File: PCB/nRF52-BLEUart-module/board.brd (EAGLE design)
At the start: 39 x 18 mm, 44 parts, among them J1 USB-A_PTH_MALE, U1 CH340E, U2 NRF52832, Y1 32MHz_2016, Y2 32.768kHz

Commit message: fixed #4
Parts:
- moved C15 1.45 mm to (30.1, 8.64), turned to 315 degrees
- moved JP1 1.40 mm to (1.52, 9.00)
- moved C16 1.09 mm to (31.6, 11.7), turned to 135 degrees
- moved L1 0.40 mm to (30.9, 10.2), turned to 45 degrees
- moved C13 0.38 mm to (29.2, 10.8)
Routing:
- net VCCIO: track 23.1 -> 24.5 mm
- net UART_RX: track 29.8 -> 31.2 mm
- net RF-1: track 4.67 -> 3.52 mm
- net UART_TX: track 28.3 -> 28.9 mm

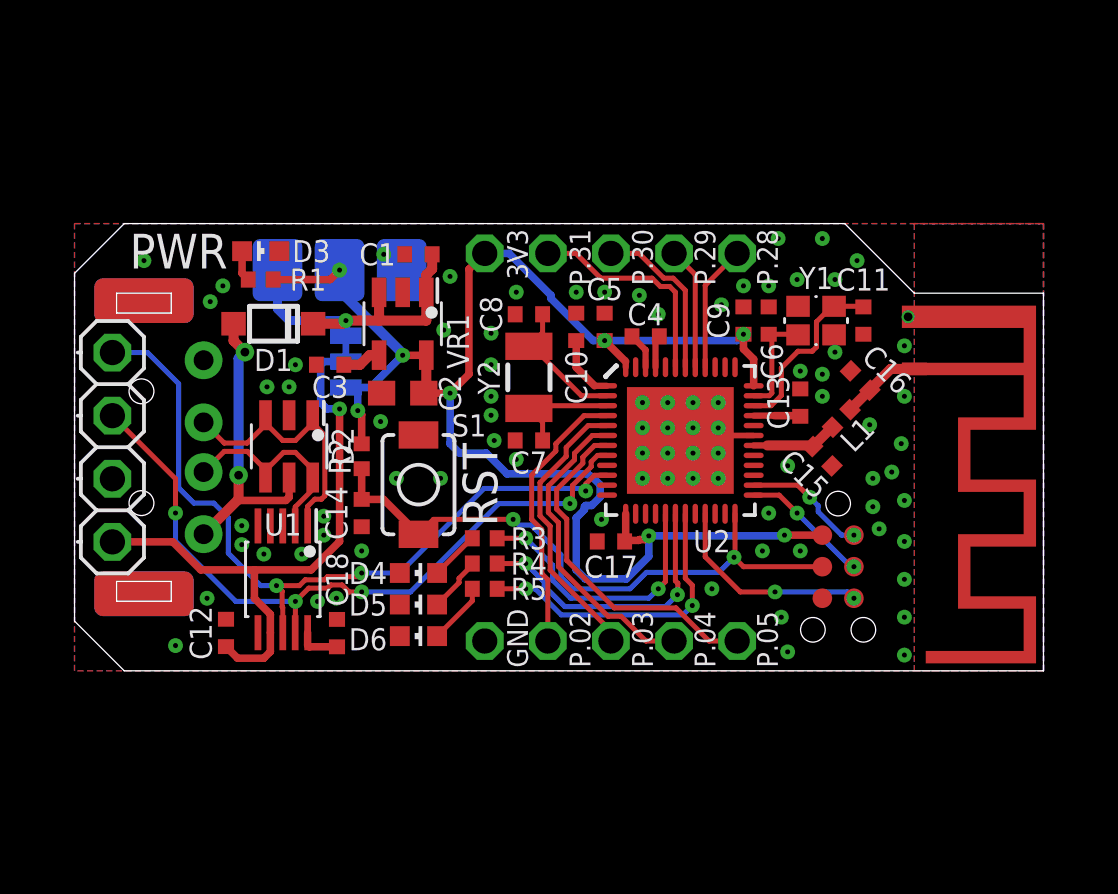
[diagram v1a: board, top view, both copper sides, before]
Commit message: fixed #2, removed unecessary power test pad
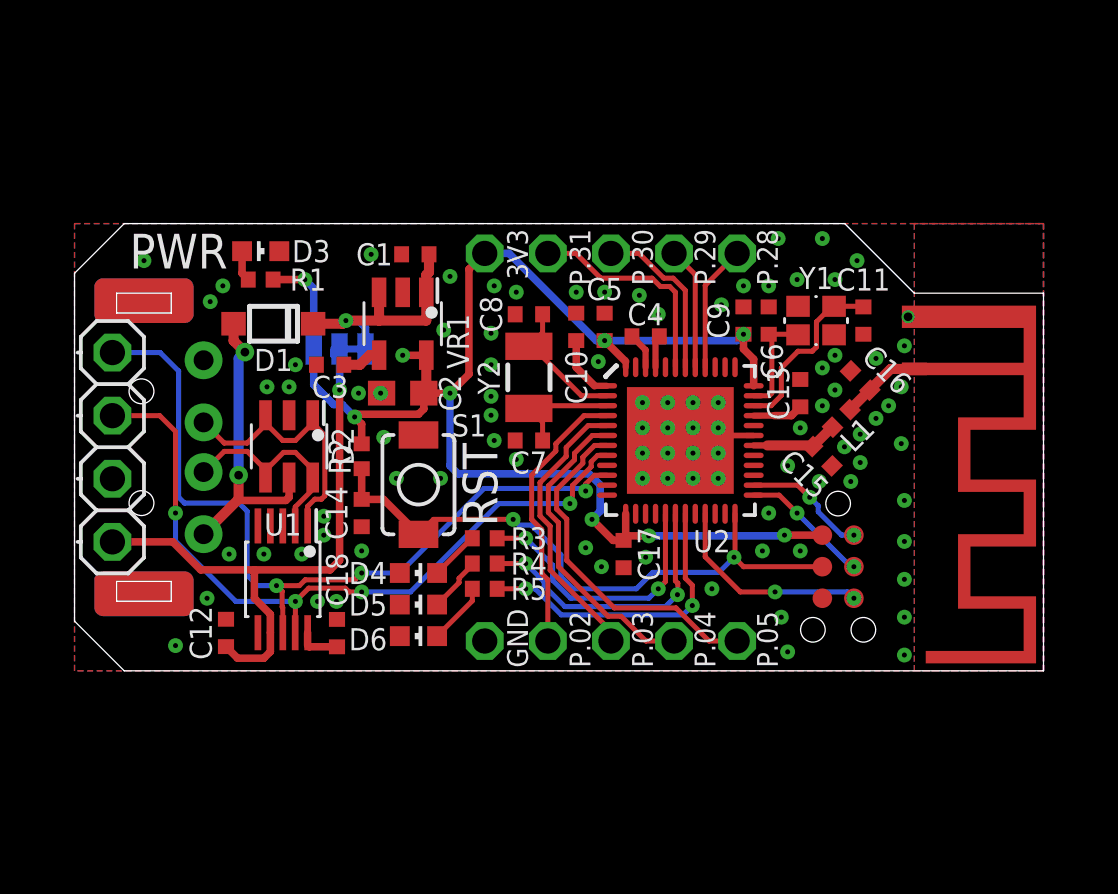
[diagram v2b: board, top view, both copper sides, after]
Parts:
- removed TP1: TEST-POINT-3, angrypig7-Tests:PAD-3X-RECT-SILK
- moved C17 0.72 mm to (22.1, 4.70), turned to 270 degrees
- moved JP2 0.57 mm to (10.7, 13.0), turned to 180 degrees
- moved C13 0.38 mm to (29.2, 11.2)
- moved C1 0.13 mm to (13.7, 16.8)
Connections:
- net 3V3: no longer TP1.P$2
- net 5V: no longer TP1.P$3
- net GND: no longer TP1.P$1
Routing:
- net 3V3: track 64.1 -> 59.6 mm, vias 8 -> 9
- net 5V: track 13.6 -> 10.2 mm
- net UART_RX: track 31.2 -> 32.4 mm
- net UART_TX: track 28.9 -> 29.9 mm
- net VCCIO: track 24.5 -> 24.0 mm
- net GND: vias 83 -> 92

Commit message: added edge rails, mousebites to the PCB. DRC error fixes needed
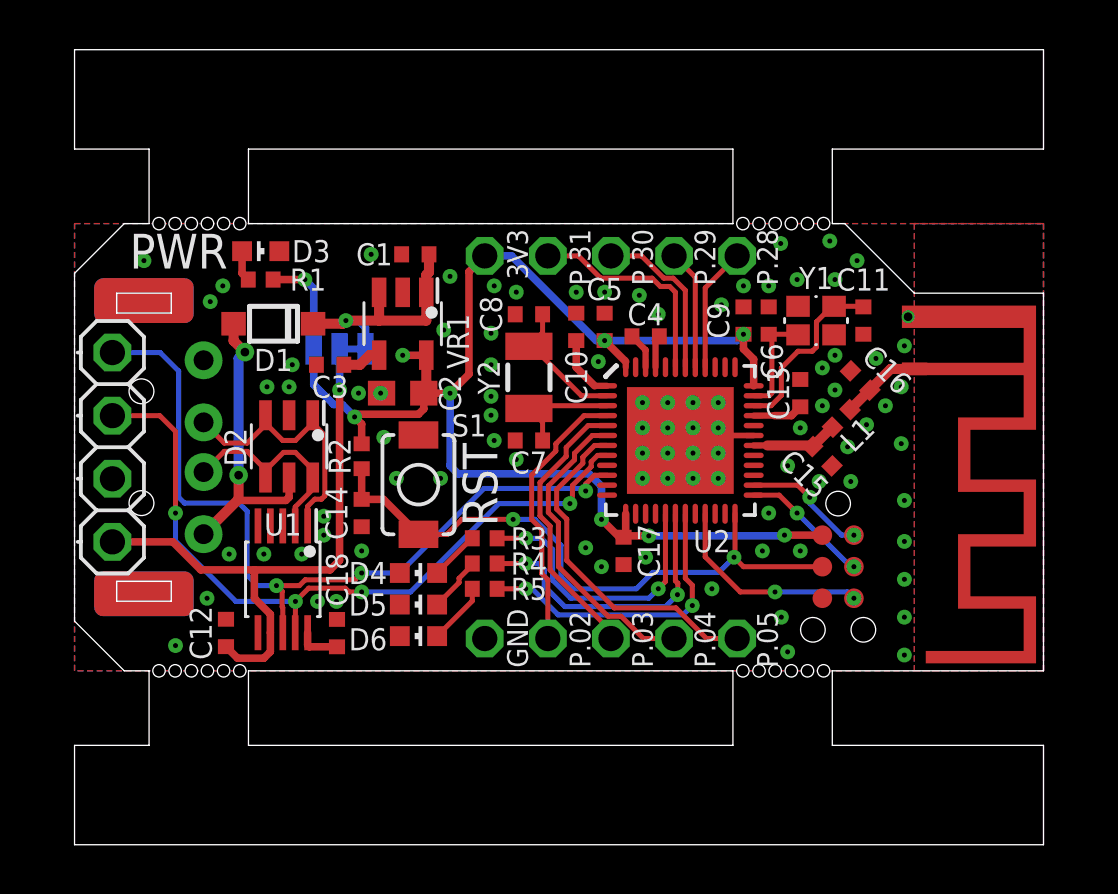
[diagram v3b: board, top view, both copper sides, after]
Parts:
- moved C17 0.13 mm to (22.1, 4.83)
- moved JP3 0.10 mm to (21.6, 16.7)
- moved JP4 0.10 mm to (21.6, 1.30)
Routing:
- net 3V3: track 59.6 -> 58.7 mm
- net GND: vias 92 -> 90
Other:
- board size 39 x 18 mm -> 39 x 32 mm

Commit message: PCB artwork, gerbers and production files - part rotation needs fixes
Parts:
- turned C12 to 270 degrees
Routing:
- net VCCIO: track 23.9 -> 23.1 mm
- net GND: vias 90 -> 88

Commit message: final PCB for V1.0
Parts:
- C15, C16: value (none) -> DNP
- JP1: device angrypig7-Connectors-PinHeads:1X04/90 -> angrypig7-Connectors-PinHeads:1X04-NOSILK
- JP2: value 3V3 5V -> 5V 3V3
- R1: value 10k -> 15k
- moved C12 1.05 mm to (6.35, 2.54)
- moved R1 0.68 mm to (8.13, 15.5)
- moved D3 0.68 mm to (8.13, 16.6)
- moved D1 0.54 mm to (8.38, 13.6)
- moved U1 0.13 mm to (8.51, 3.68)
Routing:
- net VCCIO: track 23.1 -> 22.1 mm
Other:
- board size 39 x 32 mm -> 41 x 32 mm
- board text added: ">CREVISION"

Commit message: V1.1.0 update
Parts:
- JP1: value V G Tx Rx -> Rx Tx G V
- R1: value 15k -> 7.5k
- U$1: device angrypig7-Antennas:TI-AN043_LEFT -> angrypig7-Antennas:TI-AN043_LEFT_SHORTER
- moved U$1 1.50 mm to (33.3, 16.2)
- moved C16 0.77 mm to (32.4, 11.6), turned to 315 degrees
- moved L1 0.60 mm to (30.9, 10.8)
- moved C15 0.51 mm to (30.0, 9.14)
- moved C13 0.22 mm to (29.3, 11.4)
- moved JP1 0.13 mm to (1.40, 9.03), turned to 270 degrees
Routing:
- net UART_RX: track 32.4 -> 24.8 mm
- net VCCIO: track 22.1 -> 28.4 mm, vias 1 -> 2
- net UART_TX: track 29.9 -> 27.7 mm
- net GND: vias 88 -> 86
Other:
- outline, holes or cut-outs redrawn
